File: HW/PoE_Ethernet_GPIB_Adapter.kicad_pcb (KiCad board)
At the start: 6 copper layers, 60 x 55 mm, 196 parts, among them J1 ARJM11C7-114-BA-EW2, J2 112-024-113R001, J3 USB4105-GF-A, J4 UPDI Debug Connector, Q1 PMV30XPEAR, Q2 BC857BS, SW1 Reset, U1 LM5180, U10 AZ1117-3.3_SOT89, U11 TPS2375-1, U2 ATmega4809-A, U3 W5500, U4 24AA256UID, U5 USBLC6-2P6, U6 CH340X, U7 SN74LV1T125DCK, U8 SN74LV1T125DCK, U9 APX811-31UG-7, Y1 25Mhz

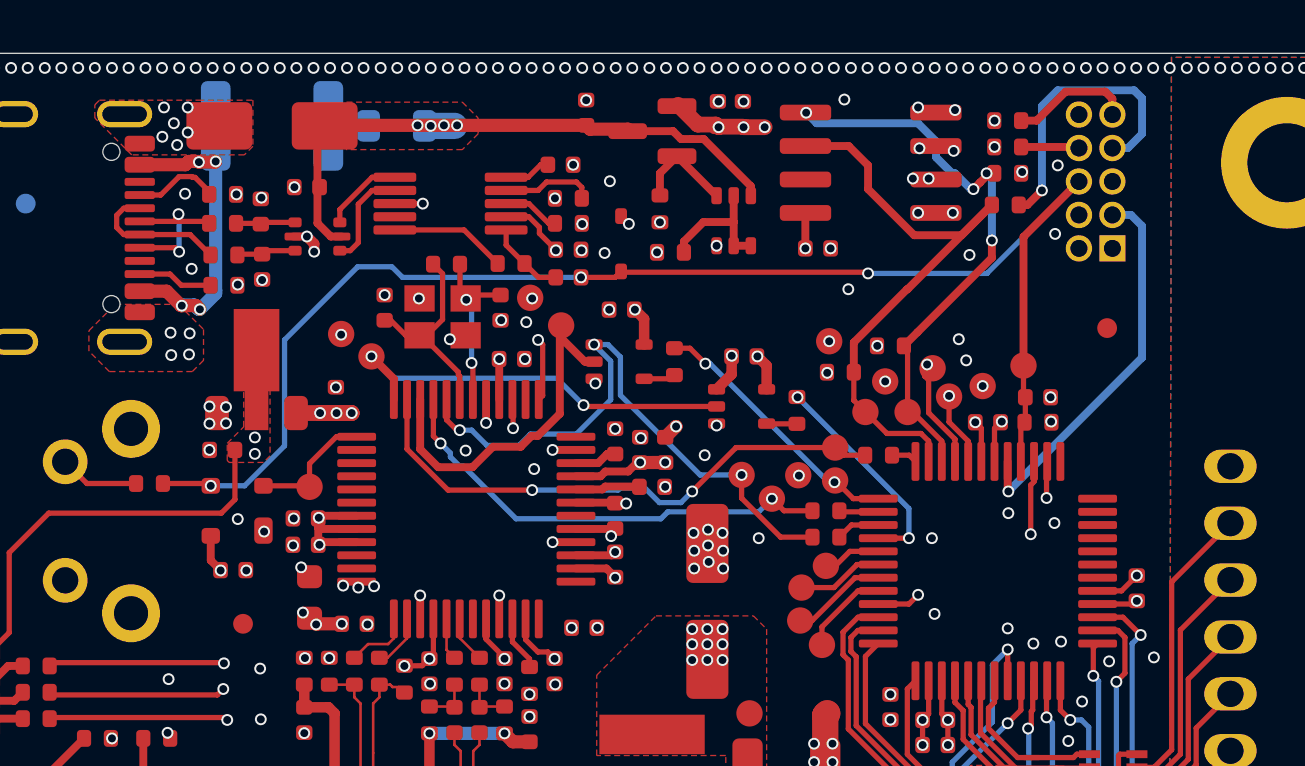
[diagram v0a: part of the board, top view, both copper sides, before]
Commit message: Added uart and i2c to jtag connector, docs added
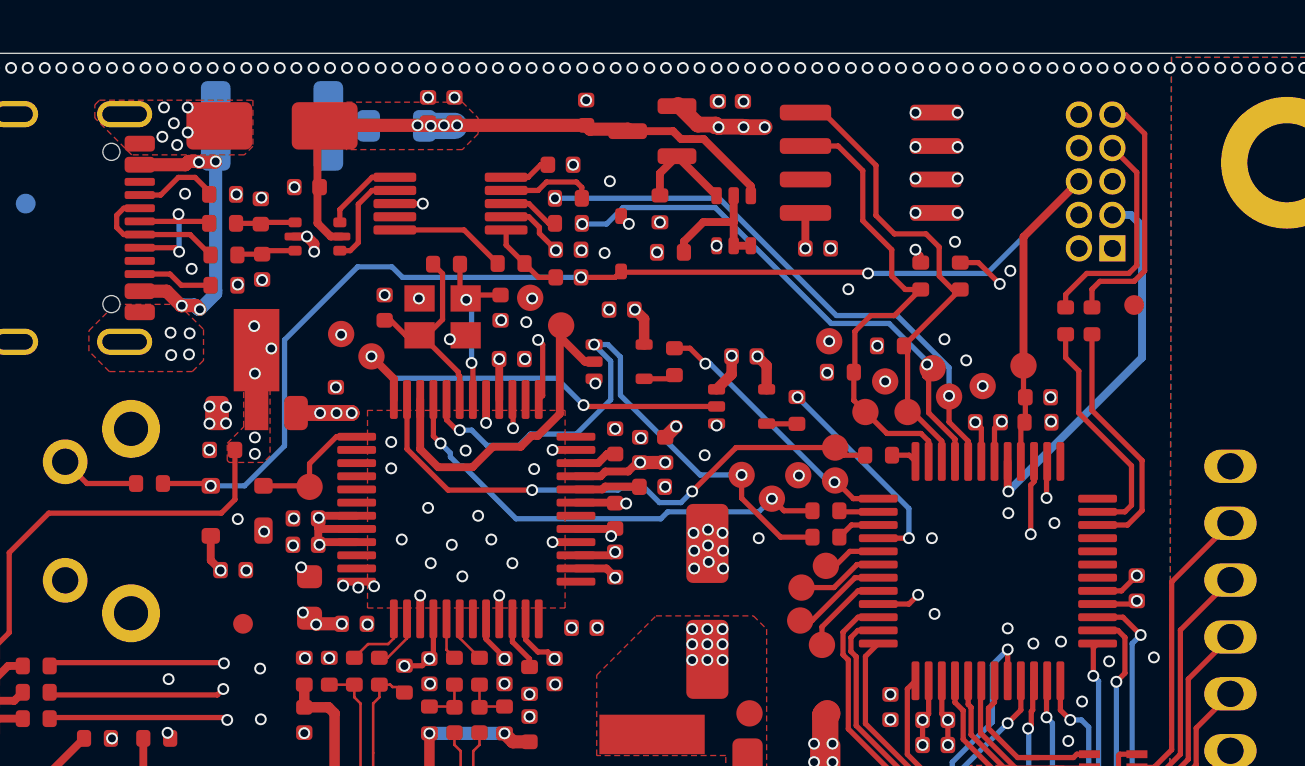
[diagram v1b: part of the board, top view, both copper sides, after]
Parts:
- added C63: 10µ, Capacitor_SMD:C_0402_1005Metric, F.Cu at (-13.4, -25.4)
- added C64: 10µ, Capacitor_SMD:C_0402_1005Metric, F.Cu at (-12.4, -25.4)
- moved R55 8.25 mm to (11.8, -17.4), turned to 90 degrees
- moved R56 6.96 mm to (10.8, -17.4), turned to 90 degrees
- moved R53 4.30 mm to (6.80, -19.1), turned to 90 degrees
- moved R54 4.19 mm to (5.30, -19.1), turned to 90 degrees
- moved FID2 1.35 mm to (13.4, -18.0)
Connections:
- J4 pad 1: unconnected-(J4-Pin_1-Pad1) -> Net-(J4-Pin_1)
- J4 pad 8: Net-(J4-Pin_8) -> unconnected-(J4-Pin_8-Pad8)
- R53 pad 2: Net-(J4-Pin_5) -> Net-(J4-Pin_1)
- R54 pad 2: Net-(J4-Pin_7) -> Net-(J4-Pin_5)
- R55 pad 1: /MCU/MCU_TX -> /MCU/MCU_TX2
- R56 pad 1: /MCU/MCU_RX -> /MCU/MCU_RX2
- R56 pad 2: Net-(J4-Pin_8) -> Net-(J4-Pin_7)
- U2 pad 34: unconnected-(U2-PF0-Pad34) -> /MCU/MCU_TX2
- U2 pad 35: unconnected-(U2-PF1-Pad35) -> /MCU/MCU_RX2
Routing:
- net /MCU/MCU_TX: track 33.3 -> 21.5 mm, vias 3 -> 2
- net /MCU/MCU_RX: track 31.8 -> 20.4 mm, vias 3 -> 2
- net /MCU/MCU_TX2: track 0.00 -> 9.39 mm
- net /MCU/MCU_RX2: track 0.00 -> 8.92 mm
- net Net-(J4-Pin_1): track 0.00 -> 7.09 mm, vias 0 -> 1
- net Net-(J4-Pin_9): track 4.63 -> 9.71 mm
- net /MCU/SCL: track 23.3 -> 18.4 mm
- net /MCU/SDA: track 22.8 -> 18.5 mm, vias 4 -> 0
- net Net-(J4-Pin_7): track 11.2 -> 8.49 mm, vias 1 -> 0
- net Net-(J4-Pin_5): track 12.3 -> 14.6 mm
- net Net-(J4-Pin_8): track 2.21 -> 0.00 mm
- net +5V: track 48.4 -> 49.9 mm, vias 29 -> 32
- net GND: vias 523 -> 533
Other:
- board text added: "PoE Ethernet GPIB Adapter"
- board text removed: "Ethernet-GPIB Adapter"

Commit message: asdf
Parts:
- turned C57 to 180 degrees
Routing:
- net Earth: track 6.68 -> 3.84 mm
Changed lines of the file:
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@@
 	(footprint "Capacitor_SMD:C_0805_2012Metric"
 		(layer "F.Cu")
-		(at 7.4 16.875)
+		(at 7.4 16.9 180)
 		(descr "Capacitor SMD 0805 (2012 Metric), square (rectangular) end terminal, IPC_7351 nominal, (Body size source: IPC-SM-782 page 76, https://www.pcb-3d.com/wordpress/wp-content/uploads/ipc-sm-782a_amendment_1_and_2.pdf, https://docs.google.com/spreadsheets/d/1BsfQQcO9C6DZCsRaXUlFlo91Tg2WpOkGARC1WS5S8t0/edit?usp=sharing), generated with kicad-footprint-generator")
 		(tags "capacitor")
 		(property "Reference" "C57"
-			(at 0 -1.68 0)
+			(at 0 -1.68 360)
 			(layer "User.1")
 			(effects
@@
 		)
 		(property "Value" "4.7n 1kV"
-			(at 0 1.68 0)
+			(at 0 1.68 360)
 			(layer "F.Fab")
 			(effects
@@
 		)
 		(property "Footprint" ""
-			(at 0 0 0)
+			(at 0 0 360)
 			(layer "F.Fab")
 			(hide yes)
@@
 		)
 		(property "Datasheet" ""
-			(at 0 0 0)
+			(at 0 0 180)
 			(unlocked yes)
 			(layer "F.Fab")
@@
 		)
 		(property "Description" "Unpolarized capacitor"
-			(at 0 0 0)
+			(at 0 0 180)
 			(unlocked yes)
 			(layer "F.Fab")
@@
 		)
 		(property "Model" "C0805C472KDRACTU"
-			(at 0 0 0)
+			(at 0 0 180)
 			(unlocked yes)
 			(layer "F.Fab")
@@
 		)
 		(property "Manufacturer" "KEMET"
-			(at 0 0 0)
+			(at 0 0 180)
 			(unlocked yes)
 			(layer "F.Fab")
@@
 		)
 		(property "JLCPCB" "C565695"
-			(at 0 0 0)
+			(at 0 0 180)
 			(unlocked yes)
 			(layer "F.Fab")
@@
 		(attr smd)
 		(fp_line
-			(start -1.7 -0.98)
-			(end 1.7 -0.98)
+			(start 1.7 0.98)
+			(end -1.7 0.98)
 			(stroke
 				(width 0.05)
@@
 		)
 		(fp_line
-			(start -1.7 0.98)
-			(end -1.7 -0.98)
+			(start 1.7 -0.98)
+			(end 1.7 0.98)
 			(stroke
 				(width 0.05)
@@
 		)
 		(fp_line
-			(start 1.7 -0.98)
-			(end 1.7 0.98)
+			(start -1.7 0.98)
+			(end -1.7 -0.98)
 			(stroke
 				(width 0.05)
@@
 		)
 		(fp_line
-			(start 1.7 0.98)
-			(end -1.7 0.98)
+			(start -1.7 -0.98)
+			(end 1.7 -0.98)
 			(stroke
 				(width 0.05)
@@
 		)
 		(fp_line
-			(start -1 -0.625)
-			(end 1 -0.625)
+			(start 1 0.625)
+			(end -1 0.625)
 			(stroke
 				(width 0.1)
@@
 		)
 		(fp_line
-			(start -1 0.625)
-			(end -1 -0.625)
+			(start 1 -0.625)
+			(end 1 0.625)
 			(stroke
 				(width 0.1)
@@
 		)
 		(fp_line
-			(start 1 -0.625)
-			(end 1 0.625)
+			(start -1 0.625)
+			(end -1 -0.625)
 			(stroke
 				(width 0.1)
@@
 		)
 		(fp_line
-			(start 1 0.625)
-			(end -1 0.625)
+			(start -1 -0.625)
+			(end 1 -0.625)
 			(stroke
 				(width 0.1)
@@
 		)
 		(fp_line
-			(start -0.261252 -0.735)
-			(end 0.261252 -0.735)
+			(start -0.261252 0.735)
+			(end 0.261252 0.735)
 			(stroke
 				(width 0.12)
@@
 		)
 		(fp_line
-			(start -0.261252 0.735)
-			(end 0.261252 0.735)
+			(start -0.261252 -0.735)
+			(end 0.261252 -0.735)
 			(stroke
 				(width 0.12)
@@
 		)
 		(fp_text user "${REFERENCE}"
-			(at 0 0 0)
+			(at 0 0 360)
 			(layer "F.Fab")
 			(effects
@@
 		)
 		(pad "1" smd roundrect
-			(at -0.95 0)
+			(at -0.95 0 180)
 			(size 1 1.45)
 			(layers "F.Cu" "F.Mask" "F.Paste")
@@
 		)
 		(pad "2" smd roundrect
-			(at 0.95 0)
+			(at 0.95 0 180)
 			(size 1 1.45)
 			(layers "F.Cu" "F.Mask" "F.Paste")
@@
 					(xy 2.562135 -23.67391) (xy 2.420116 -23.569076) (xy 2.256769 -23.480525) (xy 2.082437 -23.416511)
 					(xy 1.888964 -23.376857) (xy 1.67315 -23.363105) (xy 1.45746 -23.376857) (xy 1.26411 -23.416511)
-					(xy 1.089898 -23.480525) (xy 0.926442 -23.569094) (xy 0.78443 -23.673929) (xy 0.661803 -23.795415)
-					(xy 0.557004 -23.93306) (xy 0.469614 -24.086359) (xy 0.399486 -24.257034) (xy 0.331952 -24.526478)
-					(xy 0.309177 -24.810976) (xy 0.695325 -24.810976) (xy 0.711384 -24.579532) (xy 0.75834 -24.366027)
+					(xy 1.089898 -23.480525) (xy 0.926442 -23.569094) (xy 0.784429 -23.673929) (xy 0.661802 -23.795415)
+					(xy 0.557003 -23.93306) (xy 0.469613 -24.086359) (xy 0.399485 -24.257034) (xy 0.331951 -24.526478)
+					(xy 0.309176 -24.810976) (xy 0.695324 -24.810976) (xy 0.711383 -24.579532) (xy 0.758339 -24.366027)
 					(xy 0.837011 -24.168231) (xy 0.942986 -24.001128) (xy 1.079756 -23.862439) (xy 1.24945 -23.756397)
 					(xy 1.375374 -23.708186) (xy 1.515771 -23.6783) (xy 1.67315 -23.66792) (xy 1.830653 -23.6783) (xy 1.971173 -23.708186)
@@
 					(xy 2.097217 -25.863358) (xy 1.971056 -25.912802) (xy 1.830547 -25.94341) (xy 1.67315 -25.954033)
 					(xy 1.515877 -25.94341) (xy 1.375492 -25.912802) (xy 1.24945 -25.863358) (xy 1.079526 -25.756124)
-					(xy 0.942986 -25.618627) (xy 0.837114 -25.45336) (xy 0.75834 -25.255926) (xy 0.711384 -25.042421)
-					(xy 0.695325 -24.810976) (xy 0.309177 -24.810976) (xy 0.331952 -25.095475) (xy 0.399486 -25.364919)
-					(xy 0.469614 -25.535594) (xy 0.557004 -25.688893) (xy 0.661803 -25.826538) (xy 0.784436 -25.948009)
+					(xy 0.942986 -25.618627) (xy 0.837114 -25.45336) (xy 0.758339 -25.255926) (xy 0.711383 -25.042421)
+					(xy 0.695324 -24.810976) (xy 0.309176 -24.810976) (xy 0.331951 -25.095475) (xy 0.399485 -25.364919)
+					(xy 0.469613 -25.535594) (xy 0.557003 -25.688893) (xy 0.661802 -25.826538) (xy 0.784435 -25.948009)
 					(xy 0.926448 -26.052783) (xy 1.089898 -26.141245) (xy 1.264119 -26.205361) (xy 1.457469 -26.245075)
 					(xy 1.67315 -26.258848)
@@
 				(pts
 					(xy -1.919234 -26.20023) (xy -1.919234 -25.883691) (xy -1.096746 -25.883691) (xy -1.096746 -23.41)
-					(xy -0.710598 -23.41) (xy -0.710598 -25.883691) (xy 0.112073 -25.883691) (xy 0.112073 -26.20023)
+					(xy -0.710598 -23.41) (xy -0.710598 -25.883691) (xy 0.112072 -25.883691) (xy 0.112072 -26.20023)
 				)
 			)
@@
 	)
 	(via
+		(at 8.075 16.4)
+		(size 0.45)
+		(drill 0.3)
+		(layers "F.Cu" "B.Cu")
+		(net 1)
+	)
+	(via
 		(at 5.791994 26.9)
 		(size 0.45)
@@
 	)
 	(via
-		(at 6.75 17.35)
-		(size 0.45)
-		(drill 0.3)
-		(layers "F.Cu" "B.Cu")
-		(net 1)
-	)
-	(via
 		(at 22.4 -27)
 		(size 0.45)
@@
 	)
 	(via
+		(at 8.075 17.3)
+		(size 0.45)
+		(drill 0.3)
+		(layers "F.Cu" "B.Cu")
+		(net 1)
+	)
+	(via
 		(at -2.45 -13.425)
 		(size 0.45)
@@
 	)
 	(via
-		(at 6.75 16.425)
-		(size 0.45)
-		(drill 0.3)
-		(layers "F.Cu" "B.Cu")
-		(net 1)
-	)
-	(via
 		(at 24.929003 26.9)
 		(size 0.45)
@@
 	)
 	(segment
-		(start -13.7 -14.4125)
-		(end -13.7 -12.527979)
-		(width 0.3)
-		(layer "F.Cu")
-		(net 101)
-	)
-	(segment
-		(start -9.47 -13.032979)
-		(end -9.238901 -13.032979)
+		(start -9.65188 -12.62)
+		(end -8.4 -13.87188)
 		(width 0.3)
 		(layer "F.Cu")
@@
 	)
 	(segment
-		(start -13.017021 -11.845)
-		(end -11.714045 -11.845)
-		(width 0.3)
-		(layer "F.Cu")
-		(net 101)
-	)
-	(segment
-		(start -9.882979 -12.62)
-		(end -9.47 -13.032979)
+		(start -10.939045 -12.62)
+		(end -9.65188 -12.62)
 		(width 0.3)
 		(layer "F.Cu")
@@
 	)
 	(segment
-		(start -9.238901 -13.032979)
-		(end -8.4 -13.87188)
+		(start -11.714045 -11.845)
+		(end -10.939045 -12.62)
 		(width 0.3)
 		(layer "F.Cu")
@@
 	)
 	(segment
-		(start -11.714045 -11.845)
-		(end -10.939045 -12.62)
+		(start -13.017021 -11.845)
+		(end -11.714045 -11.845)
 		(width 0.3)
 		(layer "F.Cu")
@@
 	)
 	(segment
-		(start -8.35 -16.75)
-		(end -7.45 -15.85)
+		(start -8.4 -13.87188)
+		(end -8.4 -17.175)
 		(width 0.3)
 		(layer "F.Cu")
@@
 	)
 	(segment
-		(start -8.4 -13.87188)
-		(end -8.4 -17.175)
+		(start -8.35 -16.75)
+		(end -7.45 -15.85)
 		(width 0.3)
 		(layer "F.Cu")
@@
 	)
 	(segment
-		(start -8.35 -17.225)
-		(end -8.35 -16.75)
+		(start -13.7 -12.527979)
+		(end -13.017021 -11.845)
 		(width 0.3)
 		(layer "F.Cu")
@@
 	)
 	(segment
-		(start -13.7 -12.527979)
-		(end -13.017021 -11.845)
+		(start -13.7 -14.4125)
+		(end -13.7 -12.527979)
 		(width 0.3)
 		(layer "F.Cu")
@@
 	)
 	(segment
-		(start -10.939045 -12.62)
-		(end -9.882979 -12.62)
+		(start -8.35 -17.225)
+		(end -8.35 -16.75)
 		(width 0.3)
 		(layer "F.Cu")
@@
 	)
 	(via
-		(at 8.075 16.425)
+		(at 1.95 22)
 		(size 0.45)
 		(drill 0.3)
@@
 	)
 	(via
-		(at 1.95 22)
+		(at 2.8 23.55)
 		(size 0.45)
 		(drill 0.3)
@@
 	)
 	(via
-		(at 2.8 23.55)
+		(at 3.208006 22)
 		(size 0.45)
 		(drill 0.3)
@@
 	)
 	(via
-		(at 3.208006 22)
+		(at 6.75 17.325)
 		(size 0.45)
 		(drill 0.3)
@@
 	)
 	(via
-		(at 8.075 17.325)
-		(size 0.45)
-		(drill 0.3)
-		(layers "F.Cu" "B.Cu")
-		(net 145)
-	)
-	(via
 		(at -0.15 25.2)
 		(size 0.45)
@@
 		(net 145)
 	)
-	(segment
-		(start 7.625 16.425)
-		(end 7.625 17.375)
-		(width 0.5)
-		(layer "In4.Cu")
-		(net 145)
-	)
-	(segment
-		(start 7.625 17.375)
-		(end 7.6 17.4)
-		(width 0.5)
-		(layer "In4.Cu")
-		(net 145)
-	)
-	(segment
-		(start 8.075 16.425)
-		(end 7.625 16.425)
-		(width 0.5)
-		(layer "In4.Cu")
-		(net 145)
-	)
-	(segment
-		(start 8 17.4)
-		(end 8.075 17.325)
-		(width 0.5)
-		(layer "In4.Cu")
-		(net 145)
-	)
-	(segment
-		(start 7.6 17.4)
-		(end 8 17.4)
-		(width 0.5)
-		(layer "In4.Cu")
-		(net 145)
-	)
-	(segment
-		(start 8.075 16.425)
-		(end 8.075 17.325)
-		(width 0.5)
-		(layer "In4.Cu")
+	(via
+		(at 6.75 16.4)
+		(size 0.45)
+		(drill 0.3)
+		(layers "F.Cu" "B.Cu")
 		(net 145)
 	)

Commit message: cleaned up and added missing files
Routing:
- net Earth: track 3.84 -> 7.09 mm, vias 29 -> 28
- net VCC: vias 10 -> 11
